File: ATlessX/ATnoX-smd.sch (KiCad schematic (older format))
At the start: 31 parts, among them J1 EXT_PWR_SW, J2 ATX, J3 P8, J4 P9, SW1 Power, U1 74LS74, U2 74LS14, U3 L7905

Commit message: Fix design, update gerbers
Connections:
- net 12V is gone; now on net +12V: D5.2 (A)
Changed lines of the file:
@@
 5VSB
 Text Label 9900 2150 1    50   ~ 0
-12V
++12V
 Text Label 10000 2150 1    50   ~ 0
 -12V
@@
 Filter Caps
 $Comp
-L power:GND #PWR?
+L power:GND #PWR0117
 U 1 1 5DDE969D
 P 8150 5900
-F 0 "#PWR?" H 8150 5650 50  0001 C CNN
+F 0 "#PWR0117" H 8150 5650 50  0001 C CNN
 F 1 "GND" H 8155 5727 50  0000 C CNN
 F 2 "" H 8150 5900 50  0001 C CNN
@@
 $EndComp
 $Comp
-L power:GND #PWR?
+L power:GND #PWR0118
 U 1 1 5DE66C50
 P 8650 5750
-F 0 "#PWR?" H 8650 5500 50  0001 C CNN
+F 0 "#PWR0118" H 8650 5500 50  0001 C CNN
 F 1 "GND" V 8550 5800 50  0000 R CNN
 F 2 "" H 8650 5750 50  0001 C CNN
@@
 NoConn ~ 8550 4600
 $Comp
-L power:GND #PWR?
+L power:GND #PWR0119
 U 1 1 5DECC991
 P 10100 5700
-F 0 "#PWR?" H 10100 5450 50  0001 C CNN
+F 0 "#PWR0119" H 10100 5450 50  0001 C CNN
 F 1 "GND" V 10105 5572 50  0000 R CNN
 F 2 "" H 10100 5700 50  0001 C CNN

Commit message: Add SMD variant
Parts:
- C1, C2: footprint Capacitor_THT:CP_Radial_D6.3mm_P2.50mm -> Capacitor_SMD:CP_Elec_4x5.3
- U3: footprint Package_TO_SOT_THT:TO-220-3_Horizontal_TabDown -> Package_TO_SOT_SMD:TO-263-3_TabPin2
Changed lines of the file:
@@
 F 0 "C2" H 2041 4096 50  0000 L CNN
 F 1 "10uF" H 2041 4005 50  0000 L CNN
-F 2 "Capacitor_THT:CP_Radial_D6.3mm_P2.50mm" H 1950 4050 50  0001 C CNN
+F 2 "Capacitor_SMD:CP_Elec_4x5.3" H 1950 4050 50  0001 C CNN
 F 3 "~" H 1950 4050 50  0001 C CNN
 	1    1950 4050
@@
 F 0 "C1" H 1441 4096 50  0000 L CNN
 F 1 "1uF" H 1441 4005 50  0000 L CNN
-F 2 "Capacitor_THT:CP_Radial_D6.3mm_P2.50mm" H 1350 4050 50  0001 C CNN
+F 2 "Capacitor_SMD:CP_Elec_4x5.3" H 1350 4050 50  0001 C CNN
 F 3 "~" H 1350 4050 50  0001 C CNN
 	1    1350 4050
@@
 F 0 "U3" H 8250 1450 50  0000 C CNN
 F 1 "L7905" H 8250 1359 50  0000 C CNN
-F 2 "Package_TO_SOT_THT:TO-220-3_Horizontal_TabDown" H 8250 1400 50  0001 C CIN
+F 2 "Package_TO_SOT_SMD:TO-263-3_TabPin2" H 8250 1400 50  0001 C CIN
 F 3 "http://www.st.com/content/ccc/resource/technical/document/datasheet/c9/16/86/41/c7/2b/45/f2/CD00000450.pdf/files/CD00000450.pdf/jcr:content/translations/en.CD00000450.pdf" H 8250 1600 50  0001 C CNN
 	1    8250 1600

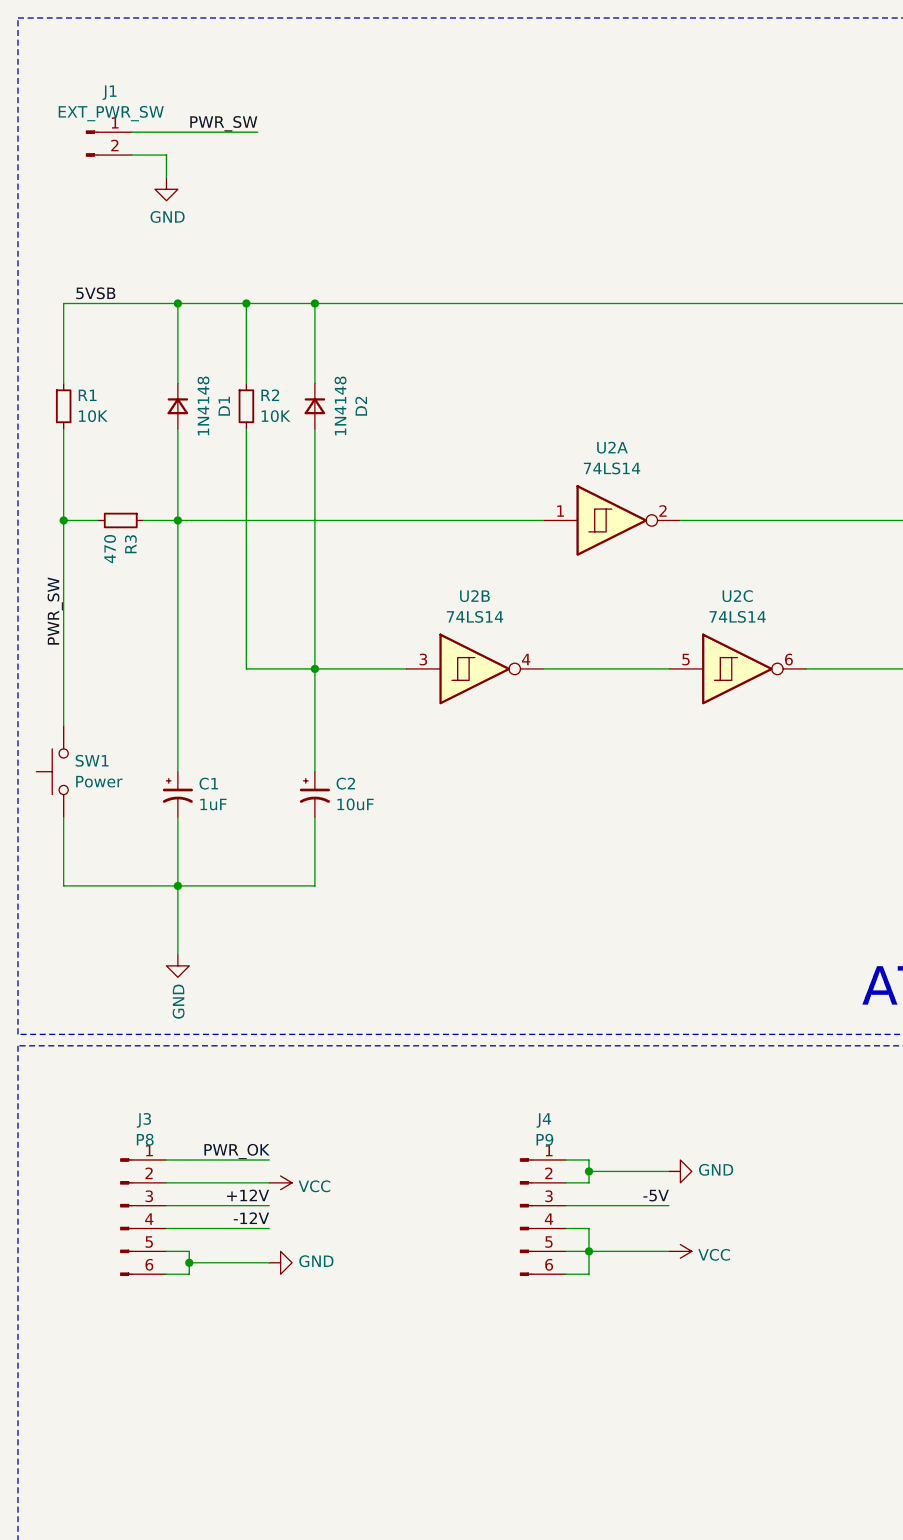
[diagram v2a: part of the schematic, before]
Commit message: Turned the SMD version into a 4layer board
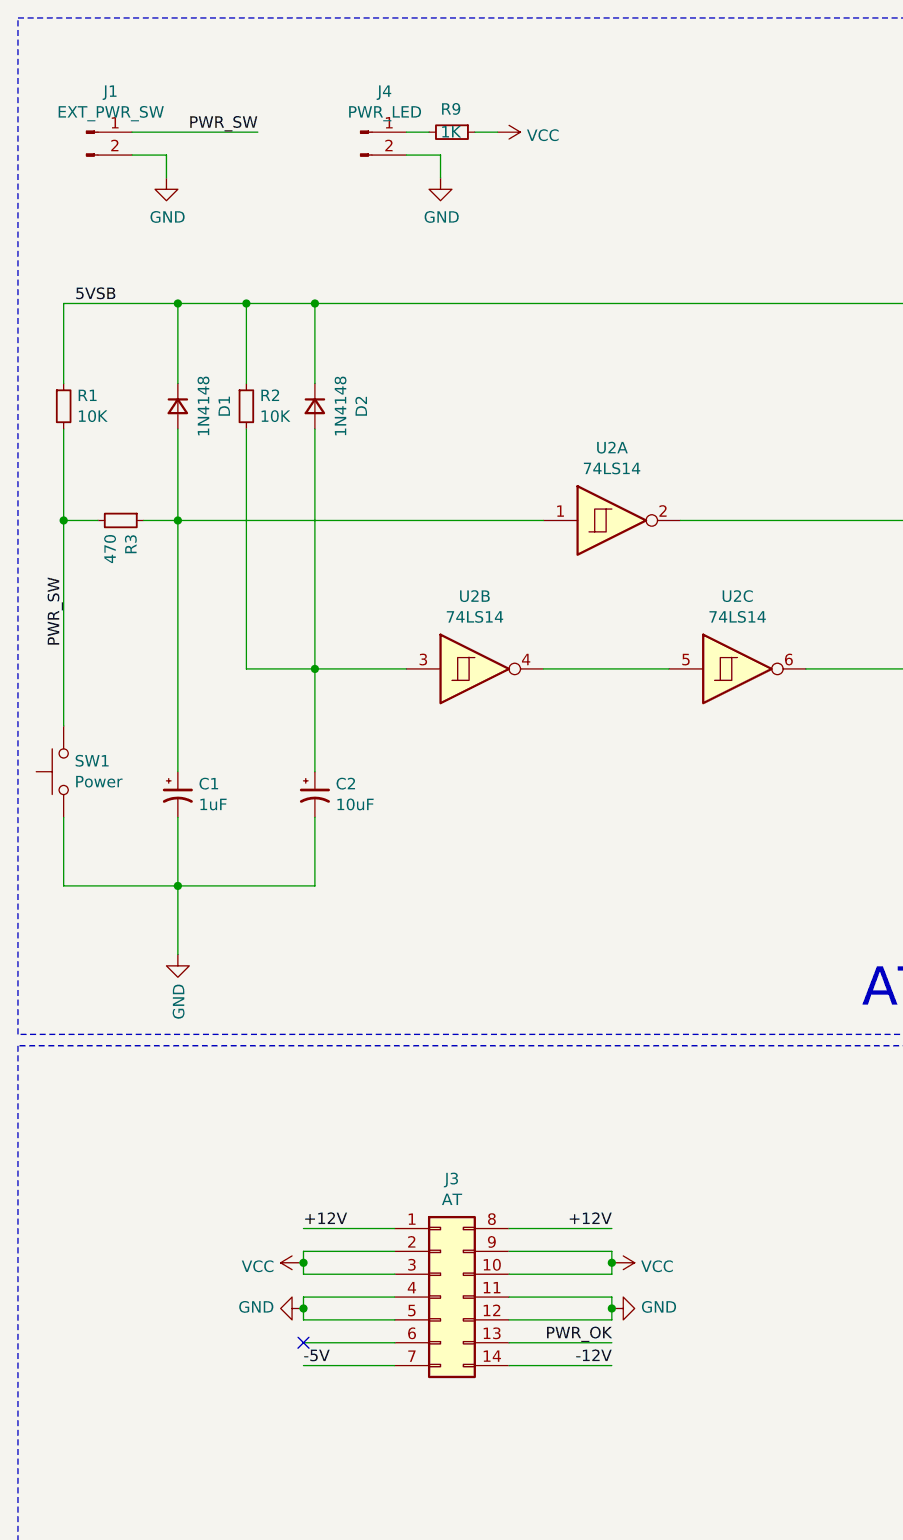
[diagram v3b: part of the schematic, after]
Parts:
- removed J3: P8, Connector_Molex:Molex_KK-254_AE-6410-06A_1x06_P2.54mm_Vertical, symbol Connector:Conn_01x06_Male
- removed J4: P9, Connector_Molex:Molex_KK-254_AE-6410-06A_1x06_P2.54mm_Vertical, symbol Connector:Conn_01x06_Male
- added J3: AT, Connector_Molex:Molex_Mini-Fit_Jr_5566-14A_2x07_P4.20mm_Vertical, symbol Connector_Generic:Conn_02x07_Top_Bottom
- added J4: PWR_LED, Connector_PinHeader_2.54mm:PinHeader_1x02_P2.54mm_Vertical, symbol Connector:Conn_01x02_Male
- added R9: 1K, Resistor_SMD:R_1206_3216Metric_Pad1.42x1.75mm_HandSolder, symbol Device:R_Small
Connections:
- net +12V: now also J3.1 (Pin_1), J3.8 (Pin_8)
- net -12V: now also J3.14 (Pin_14)
- net -5V: now also J3.7 (Pin_7)
- net GND: now also J3.11 (Pin_11), J3.12 (Pin_12), J3.4 (Pin_4), J3.5 (Pin_5), J4.2 (Pin_2)
- net PWR_OK: now also J3.13 (Pin_13)
- net VCC: now also J3.10 (Pin_10), J3.2 (Pin_2), J3.3 (Pin_3), J3.9 (Pin_9), R9.1
- new net: J4.1 (Pin_1), R9.2
- no-connect marks 11 -> 12
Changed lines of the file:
@@
 Text Label 8250 3950 0    50   ~ 0
 PWR_OK
-$Comp
-L Connector:Conn_01x06_Male J3
-U 1 1 5DDBB6AF
-P 1100 5850
-F 0 "J3" H 1206 6228 50  0000 C CNN
-F 1 "P8" H 1206 6137 50  0000 C CNN
-F 2 "Connector_Molex:Molex_KK-254_AE-6410-06A_1x06_P2.54mm_Vertical" H 1100 5850 50  0001 C CNN
-F 3 "~" H 1100 5850 50  0001 C CNN
-	1    1100 5850
-	1    0    0    -1
-$EndComp
-$Comp
-L Connector:Conn_01x06_Male J4
-U 1 1 5DDBB718
-P 2850 5850
-F 0 "J4" H 2956 6228 50  0000 C CNN
-F 1 "P9" H 2956 6137 50  0000 C CNN
-F 2 "Connector_Molex:Molex_KK-254_AE-6410-06A_1x06_P2.54mm_Vertical" H 2850 5850 50  0001 C CNN
-F 3 "~" H 2850 5850 50  0001 C CNN
-	1    2850 5850
-	1    0    0    -1
-$EndComp
-Wire Wire Line
-	1300 5650 1750 5650
-Text Label 1750 5650 2    50   ~ 0
+Text Label 3250 6450 2    50   ~ 0
 PWR_OK
-$Comp
-L power:VCC #PWR0112
-U 1 1 5DD99954
-P 1750 5750
-F 0 "#PWR0112" H 1750 5600 50  0001 C CNN
-F 1 "VCC" V 1767 5878 50  0000 L CNN
-F 2 "" H 1750 5750 50  0001 C CNN
-F 3 "" H 1750 5750 50  0001 C CNN
-	1    1750 5750
-	0    1    1    0
-$EndComp
-Wire Wire Line
-	1300 5750 1750 5750
-Wire Wire Line
-	1300 5850 1750 5850
-Wire Wire Line
-	1300 5950 1750 5950
-Text Label 1750 5850 2    50   ~ 0
+Text Label 1900 5950 0    50   ~ 0
 +12V
-Text Label 1750 5950 2    50   ~ 0
+Text Label 3250 6550 2    50   ~ 0
 -12V
 $Comp
 L power:GND #PWR0113
 U 1 1 5DDA43EF
-P 1750 6100
-F 0 "#PWR0113" H 1750 5850 50  0001 C CNN
-F 1 "GND" V 1755 5972 50  0000 R CNN
-F 2 "" H 1750 6100 50  0001 C CNN
-F 3 "" H 1750 6100 50  0001 C CNN
-	1    1750 6100
+P 3250 6300
+F 0 "#PWR0113" H 3250 6050 50  0001 C CNN
+F 1 "GND" V 3255 6172 50  0000 R CNN
+F 2 "" H 3250 6300 50  0001 C CNN
+F 3 "" H 3250 6300 50  0001 C CNN
+	1    3250 6300
 	0    -1   -1   0
 $EndComp
-Wire Wire Line
-	1300 6050 1400 6050
-Wire Wire Line
-	1400 6050 1400 6100
-Wire Wire Line
-	1400 6150 1300 6150
-Wire Wire Line
-	1400 6100 1750 6100
-Connection ~ 1400 6100
-Wire Wire Line
-	1400 6100 1400 6150
 $Comp
 L power:GND #PWR0114
 U 1 1 5DDACF0F
-P 3500 5700
-F 0 "#PWR0114" H 3500 5450 50  0001 C CNN
-F 1 "GND" V 3505 5572 50  0000 R CNN
-F 2 "" H 3500 5700 50  0001 C CNN
-F 3 "" H 3500 5700 50  0001 C CNN
-	1    3500 5700
-	0    -1   -1   0
-$EndComp
-Wire Wire Line
-	3050 5650 3150 5650
-Wire Wire Line
-	3150 5650 3150 5700
-Wire Wire Line
-	3150 5750 3050 5750
-Wire Wire Line
-	3150 5700 3500 5700
-Connection ~ 3150 5700
-Wire Wire Line
-	3150 5700 3150 5750
-Wire Wire Line
-	3050 5850 3500 5850
-Text Label 3500 5850 2    50   ~ 0
+P 1900 6300
+F 0 "#PWR0114" H 1900 6050 50  0001 C CNN
+F 1 "GND" V 1905 6172 50  0000 R CNN
+F 2 "" H 1900 6300 50  0001 C CNN
+F 3 "" H 1900 6300 50  0001 C CNN
+	1    1900 6300
+	0    1    -1   0
+$EndComp
+Text Label 1900 6550 0    50   ~ 0
 -5V
 $Comp
 L power:VCC #PWR0115
 U 1 1 5DDB7431
-P 3500 6050
-F 0 "#PWR0115" H 3500 5900 50  0001 C CNN
-F 1 "VCC" V 3517 6178 50  0000 L CNN
-F 2 "" H 3500 6050 50  0001 C CNN
-F 3 "" H 3500 6050 50  0001 C CNN
-	1    3500 6050
+P 3250 6100
+F 0 "#PWR0115" H 3250 5950 50  0001 C CNN
+F 1 "VCC" V 3267 6228 50  0000 L CNN
+F 2 "" H 3250 6100 50  0001 C CNN
+F 3 "" H 3250 6100 50  0001 C CNN
+	1    3250 6100
 	0    1    1    0
 $EndComp
-Wire Wire Line
-	3050 6050 3150 6050
-Wire Wire Line
-	3050 5950 3150 5950
-Wire Wire Line
-	3150 5950 3150 6050
-Connection ~ 3150 6050
-Wire Wire Line
-	3150 6050 3500 6050
-Wire Wire Line
-	3050 6150 3150 6150
-Wire Wire Line
-	3150 6150 3150 6050
 Wire Notes Line
 	650  5150 650  7700
@@
 Wire Wire Line
 	9800 1200 9900 1200
+$Comp
+L Connector_Generic:Conn_02x07_Top_Bottom J3
+U 1 1 5F276A3E
+P 2500 6250
+F 0 "J3" H 2550 6767 50  0000 C CNN
+F 1 "AT" H 2550 6676 50  0000 C CNN
+F 2 "Connector_Molex:Molex_Mini-Fit_Jr_5566-14A_2x07_P4.20mm_Vertical" H 2500 6250 50  0001 C CNN
+F 3 "~" H 2500 6250 50  0001 C CNN
+	1    2500 6250
+	1    0    0    -1
+$EndComp
+Wire Wire Line
+	2300 5950 1900 5950
+Wire Wire Line
+	2300 6050 1900 6050
+Wire Wire Line
+	2300 6150 1900 6150
+Wire Wire Line
+	2300 6250 1900 6250
+Wire Wire Line
+	2300 6350 1900 6350
+Wire Wire Line
+	2300 6450 1900 6450
+Wire Wire Line
+	2300 6550 1900 6550
+Wire Wire Line
+	2800 5950 3250 5950
+Wire Wire Line
+	2800 6050 3250 6050
+Wire Wire Line
+	2800 6150 3250 6150
+Wire Wire Line
+	2800 6250 3250 6250
+Wire Wire Line
+	2800 6350 3250 6350
+Wire Wire Line
+	2800 6450 3250 6450
+Wire Wire Line
+	2800 6550 3250 6550
+$Comp
+L power:VCC #PWR0112
+U 1 1 5DD99954
+P 1900 6100
+F 0 "#PWR0112" H 1900 5950 50  0001 C CNN
+F 1 "VCC" V 1917 6228 50  0000 L CNN
+F 2 "" H 1900 6100 50  0001 C CNN
+F 3 "" H 1900 6100 50  0001 C CNN
+	1    1900 6100
+	0    -1   1    0
+$EndComp
+Wire Wire Line
+	1900 6100 1900 6050
+Wire Wire Line
+	1900 6100 1900 6150
+Connection ~ 1900 6100
+Wire Wire Line
+	1900 6250 1900 6300
+Wire Wire Line
+	1900 6300 1900 6350
+Connection ~ 1900 6300
+NoConn ~ 1900 6450
+Text Label 3250 5950 2    50   ~ 0
++12V
+Wire Wire Line
+	3250 6050 3250 6100
+Wire Wire Line
+	3250 6150 3250 6100
+Connection ~ 3250 6100
+Wire Wire Line
+	3250 6250 3250 6300
+Wire Wire Line
+	3250 6350 3250 6300
+Connection ~ 3250 6300
+$Comp
+L Connector:Conn_01x02_Male J4
+U 1 1 5F28CC3D
+P 2150 1150
+F 0 "J4" H 2256 1328 50  0000 C CNN
+F 1 "PWR_LED" H 2256 1237 50  0000 C CNN
+F 2 "Connector_PinHeader_2.54mm:PinHeader_1x02_P2.54mm_Vertical" H 2150 1150 50  0001 C CNN
+F 3 "~" H 2150 1150 50  0001 C CNN
+	1    2150 1150
+	1    0    0    -1
+$EndComp
+$Comp
+L power:GND #PWR?
+U 1 1 5F28D824
+P 2500 1350
+F 0 "#PWR?" H 2500 1100 50  0001 C CNN
+F 1 "GND" H 2505 1177 50  0000 C CNN
+F 2 "" H 2500 1350 50  0001 C CNN
+F 3 "" H 2500 1350 50  0001 C CNN
+	1    2500 1350
+	1    0    0    -1
+$EndComp
+Wire Wire Line
+	2350 1250 2500 1250
+Wire Wire Line
+	2500 1250 2500 1350
+$Comp
+L Device:R_Small R9
+U 1 1 5F296280
+P 2550 1150
+F 0 "R9" V 2450 1100 50  0000 L CNN
+F 1 "1K" V 2550 1100 50  0000 L CNN
+F 2 "Resistor_SMD:R_1206_3216Metric_Pad1.42x1.75mm_HandSolder" H 2550 1150 50  0001 C CNN
+F 3 "~" H 2550 1150 50  0001 C CNN
+	1    2550 1150
+	0    1    1    0
+$EndComp
+Wire Wire Line
+	2350 1150 2450 1150
+$Comp
+L power:VCC #PWR?
+U 1 1 5F2AA769
+P 2750 1150
+F 0 "#PWR?" H 2750 1000 50  0001 C CNN
+F 1 "VCC" V 2765 1278 50  0000 L CNN
+F 2 "" H 2750 1150 50  0001 C CNN
+F 3 "" H 2750 1150 50  0001 C CNN
+	1    2750 1150
+	0    1    1    0
+$EndComp
+Wire Wire Line
+	2650 1150 2750 1150
 $EndSCHEMATC

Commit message: Add rev. 2.5 of SMD variant
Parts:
- J2: footprint Connector_Molex:Molex_Mini-Fit_Jr_5566-20A_2x10_P4.20mm_Vertical -> Connector_Molex:Molex_Mini-Fit_Jr_5569-20A2_2x10_P4.20mm_Horizontal
- J3: footprint Connector_Molex:Molex_Mini-Fit_Jr_5566-14A_2x07_P4.20mm_Vertical -> Connector_Molex:Molex_Mini-Fit_Jr_5569-14A2_2x07_P4.20mm_Horizontal
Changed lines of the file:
@@
 F 0 "J2" H 9050 4267 50  0000 C CNN
 F 1 "ATX" H 9050 4176 50  0000 C CNN
-F 2 "Connector_Molex:Molex_Mini-Fit_Jr_5566-20A_2x10_P4.20mm_Vertical" H 9000 3650 50  0001 C CNN
+F 2 "Connector_Molex:Molex_Mini-Fit_Jr_5569-20A2_2x10_P4.20mm_Horizontal" H 9000 3650 50  0001 C CNN
 F 3 "~" H 9000 3650 50  0001 C CNN
 	1    9000 3650
@@
 F 0 "J3" H 2550 6767 50  0000 C CNN
 F 1 "AT" H 2550 6676 50  0000 C CNN
-F 2 "Connector_Molex:Molex_Mini-Fit_Jr_5566-14A_2x07_P4.20mm_Vertical" H 2500 6250 50  0001 C CNN
+F 2 "Connector_Molex:Molex_Mini-Fit_Jr_5569-14A2_2x07_P4.20mm_Horizontal" H 2500 6250 50  0001 C CNN
 F 3 "~" H 2500 6250 50  0001 C CNN
 	1    2500 6250

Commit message: Rev 3
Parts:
- added C5, C6: 100nF, Capacitor_SMD:C_1206_3216Metric_Pad1.42x1.75mm_HandSolder, symbol Device:C_Small
- added C7, C8: 6.8pF, Capacitor_SMD:C_1206_3216Metric_Pad1.42x1.75mm_HandSolder, symbol Device:C_Small
- added R10: 100K, Resistor_SMD:R_1206_3216Metric_Pad1.42x1.75mm_HandSolder, symbol Device:R_Small
- added R11: 10M, Resistor_SMD:R_1206_3216Metric_Pad1.42x1.75mm_HandSolder, symbol Device:R_Small
- added U4: 74HCT4060, Package_SO:SOIC-16_3.9x9.9mm_P1.27mm, symbol logic-4000:4060-SO
- added U5: 74HC73, Package_SO:SOIC-14_3.9x8.7mm_P1.27mm, symbol 74xx:74LS73
- added Y1: 3.2768, Crystal:Crystal_SMD_HC49-SD, symbol Device:Crystal_Small
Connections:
- net GND: now also C5.1, C6.1, C7.2, C8.2, U4.12 (MR), U4.8 (GND), U5.11 (GND)
- net VCC: now also C5.2, C6.2, U4.16 (V+), U5.10 (K), U5.14 (J), U5.2 (~R), U5.3 (K), U5.4 (VCC), U5.6 (~R), U5.7 (J)
- net TICK: now reaches J3.6 (Pin_6)
- net TICK: now also U5.9 (Q)
- new net: C8.1, R11.1, U4.10 (RTC), Y1.1
- new net: R10.1, R11.2, U4.11 (RS)
- new net: U4.7 (Q3), U5.1 (C)
- new net: C7.1, R10.2, Y1.2
- new net: U5.12 (Q), U5.5 (C)
- no-connect marks 12 -> 11
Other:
- note added: "Crystal can be:\n- 3.2768Mhz to get 50Hz output\n- 3.93216Mhz to get 60Hz output"
- note added: "Ext Power"
- note removed: "AT Connectors"
- moved on the sheet: C3, C4, J3

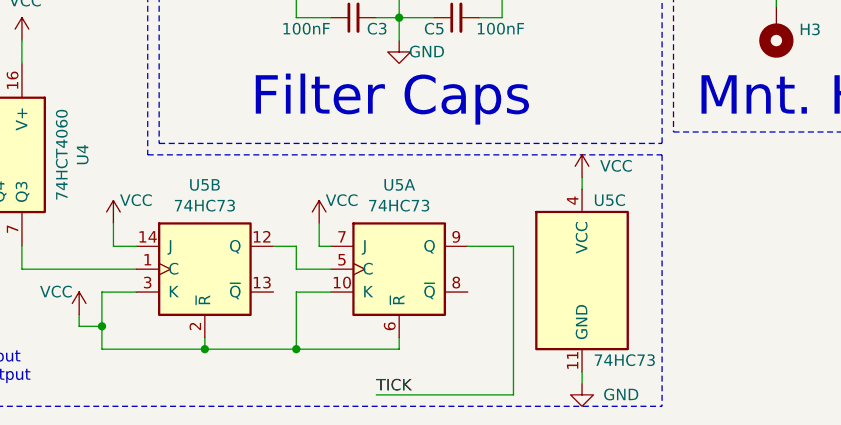
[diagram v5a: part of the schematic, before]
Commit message: Add silkscreen text
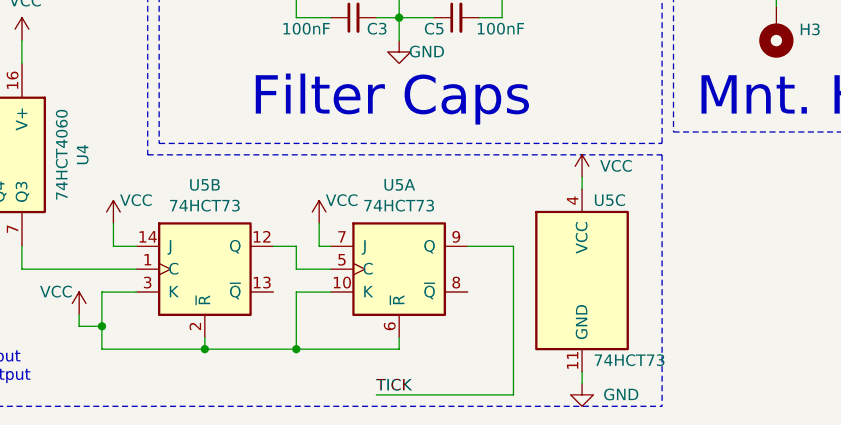
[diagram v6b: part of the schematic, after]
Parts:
- U5: value 74HC73 -> 74HCT73
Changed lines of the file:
@@
 P 5650 7100
 F 0 "U5" H 5650 7467 50  0000 C CNN
-F 1 "74HC73" H 5650 7376 50  0000 C CNN
+F 1 "74HCT73" H 5650 7376 50  0000 C CNN
 F 2 "Package_SO:SOIC-14_3.9x8.7mm_P1.27mm" H 5650 7100 50  0001 C CNN
 F 3 "http://www.ti.com/lit/gpn/sn74LS73" H 5650 7100 50  0001 C CNN
@@
 P 4800 7100
 F 0 "U5" H 4800 7467 50  0000 C CNN
-F 1 "74HC73" H 4800 7376 50  0000 C CNN
+F 1 "74HCT73" H 4800 7376 50  0000 C CNN
 F 2 "Package_SO:SOIC-14_3.9x8.7mm_P1.27mm" H 4800 7100 50  0001 C CNN
 F 3 "http://www.ti.com/lit/gpn/sn74LS73" H 4800 7100 50  0001 C CNN
@@
 P 6450 7150
 F 0 "U5" H 6500 7500 50  0000 L CNN
-F 1 "74HC73" H 6500 6800 50  0000 L CNN
+F 1 "74HCT73" H 6500 6800 50  0000 L CNN
 F 2 "Package_SO:SOIC-14_3.9x8.7mm_P1.27mm" H 6450 7150 50  0001 C CNN
 F 3 "http://www.ti.com/lit/gpn/sn74LS73" H 6450 7150 50  0001 C CNN
